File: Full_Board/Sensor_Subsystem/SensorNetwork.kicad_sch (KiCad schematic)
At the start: 32 parts, among them IC5 CD74HC4051PWT, IC6 CD74HC4051PWT, J10 OQ0432500000G, J11 OQ0432500000G, J12 OQ0432500000G, J13 OQ0432500000G, J14 OQ0432500000G, J15 OQ0432500000G, J16 OQ0432500000G, J9 OQ0432500000G

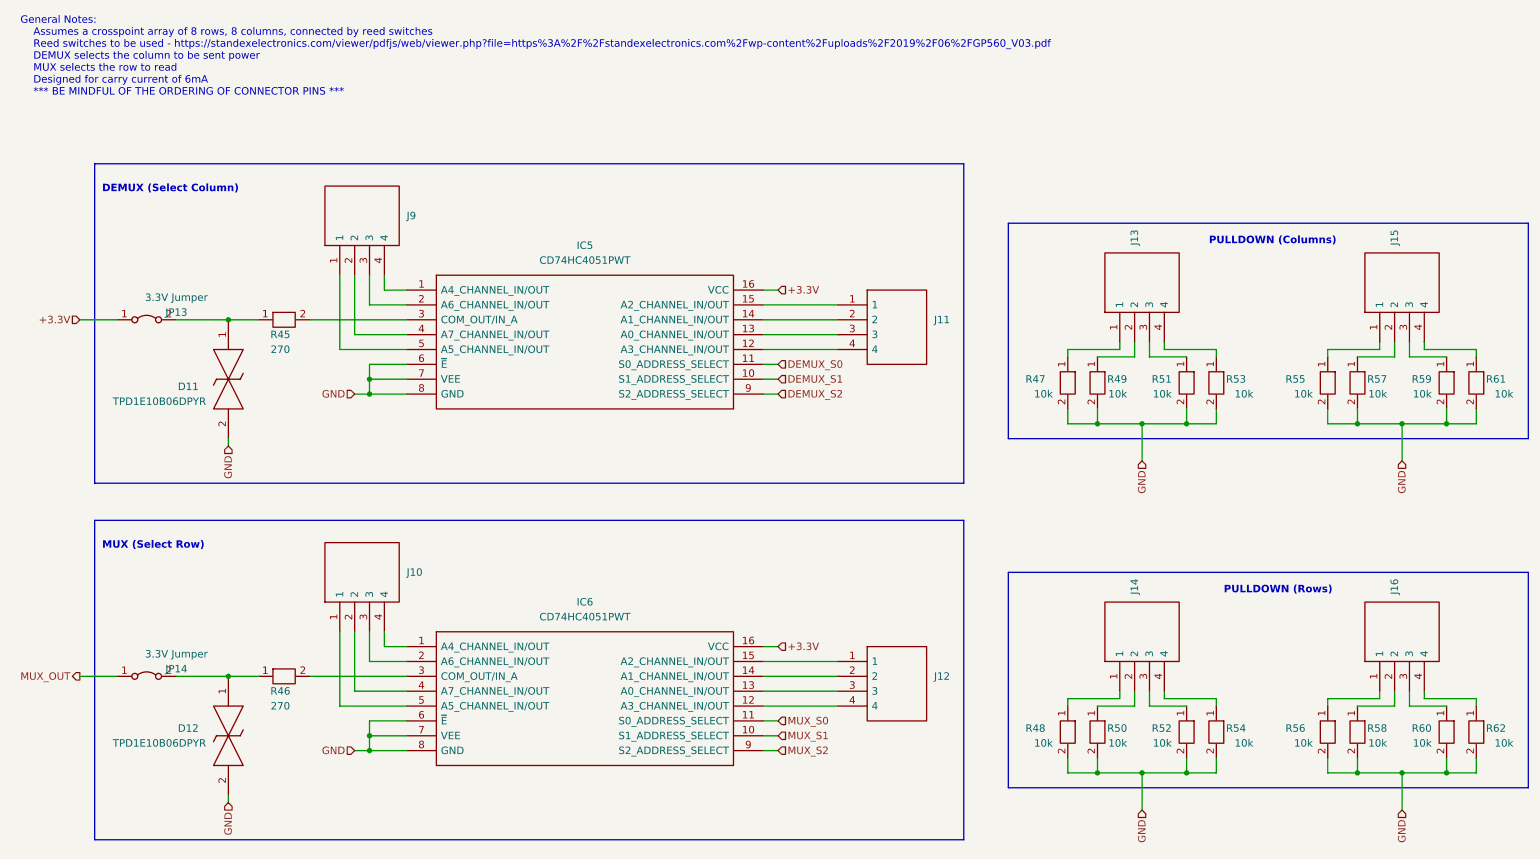
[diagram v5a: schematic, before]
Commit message: Resolve misconfigured components, replace PCB from now completed schematic
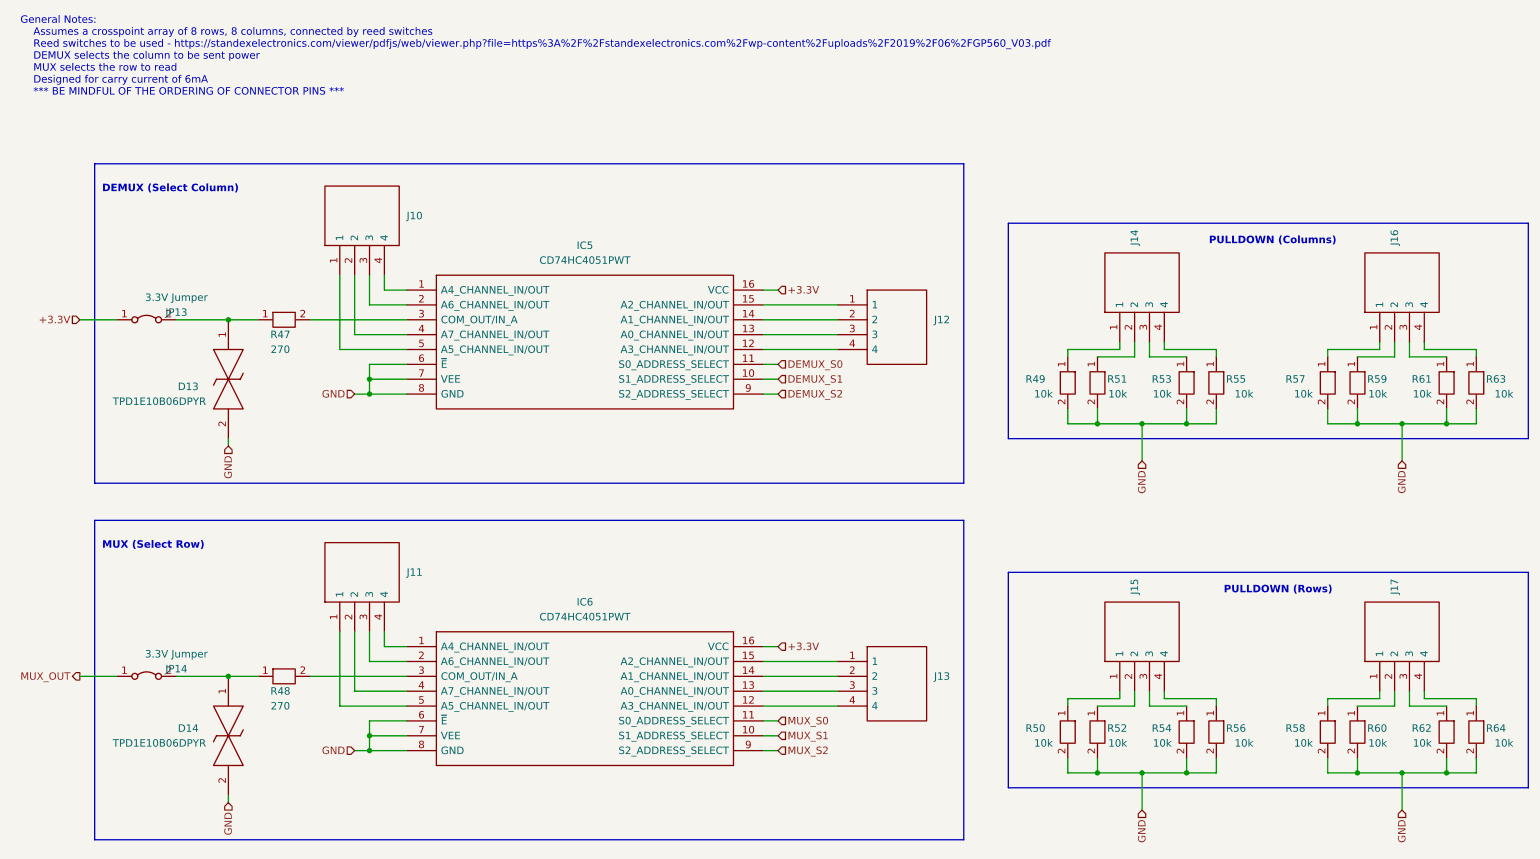
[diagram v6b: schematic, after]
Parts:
- R49: renamed from R47; footprint RESC3225X74N -> RMCF1206FT10K0:RMCF1206FT10K0; Digikey link https://www.digikey.com/en/products/detail/stackpole-electronics-inc/RMCF1206FT10K0/1759669?s=N4IgTCBcDaIEoFkDCAxAjGADANhQFTUwGlMQBdAXyA -> https://www.digikey.com/en/products/detail/stackpole-electronics-inc/RMCF1206FT10K0/1759669
- R50: renamed from R48; footprint RESC3225X74N -> RMCF1206FT10K0:RMCF1206FT10K0; Digikey link https://www.digikey.com/en/products/detail/stackpole-electronics-inc/RMCF1206FT10K0/1759669?s=N4IgTCBcDaIEoFkDCAxAjGADANhQFTUwGlMQBdAXyA -> https://www.digikey.com/en/products/detail/stackpole-electronics-inc/RMCF1206FT10K0/1759669
- R51: renamed from R49; footprint RESC3225X74N -> RMCF1206FT10K0:RMCF1206FT10K0; Digikey link https://www.digikey.com/en/products/detail/stackpole-electronics-inc/RMCF1206FT10K0/1759669?s=N4IgTCBcDaIEoFkDCAxAjGADANhQFTUwGlMQBdAXyA -> https://www.digikey.com/en/products/detail/stackpole-electronics-inc/RMCF1206FT10K0/1759669
- R52: renamed from R50; footprint RESC3225X74N -> RMCF1206FT10K0:RMCF1206FT10K0; Digikey link https://www.digikey.com/en/products/detail/stackpole-electronics-inc/RMCF1206FT10K0/1759669?s=N4IgTCBcDaIEoFkDCAxAjGADANhQFTUwGlMQBdAXyA -> https://www.digikey.com/en/products/detail/stackpole-electronics-inc/RMCF1206FT10K0/1759669
- R53: renamed from R51; footprint RESC3225X74N -> RMCF1206FT10K0:RMCF1206FT10K0; Digikey link https://www.digikey.com/en/products/detail/stackpole-electronics-inc/RMCF1206FT10K0/1759669?s=N4IgTCBcDaIEoFkDCAxAjGADANhQFTUwGlMQBdAXyA -> https://www.digikey.com/en/products/detail/stackpole-electronics-inc/RMCF1206FT10K0/1759669
- R54: renamed from R52; footprint RESC3225X74N -> RMCF1206FT10K0:RMCF1206FT10K0; Digikey link https://www.digikey.com/en/products/detail/stackpole-electronics-inc/RMCF1206FT10K0/1759669?s=N4IgTCBcDaIEoFkDCAxAjGADANhQFTUwGlMQBdAXyA -> https://www.digikey.com/en/products/detail/stackpole-electronics-inc/RMCF1206FT10K0/1759669
- R55: renamed from R53; footprint RESC3225X74N -> RMCF1206FT10K0:RMCF1206FT10K0; Digikey link https://www.digikey.com/en/products/detail/stackpole-electronics-inc/RMCF1206FT10K0/1759669?s=N4IgTCBcDaIEoFkDCAxAjGADANhQFTUwGlMQBdAXyA -> https://www.digikey.com/en/products/detail/stackpole-electronics-inc/RMCF1206FT10K0/1759669
- R56: renamed from R54; footprint RESC3225X74N -> RMCF1206FT10K0:RMCF1206FT10K0; Digikey link https://www.digikey.com/en/products/detail/stackpole-electronics-inc/RMCF1206FT10K0/1759669?s=N4IgTCBcDaIEoFkDCAxAjGADANhQFTUwGlMQBdAXyA -> https://www.digikey.com/en/products/detail/stackpole-electronics-inc/RMCF1206FT10K0/1759669
- R57: renamed from R55; footprint RESC3225X74N -> RMCF1206FT10K0:RMCF1206FT10K0; Digikey link https://www.digikey.com/en/products/detail/stackpole-electronics-inc/RMCF1206FT10K0/1759669?s=N4IgTCBcDaIEoFkDCAxAjGADANhQFTUwGlMQBdAXyA -> https://www.digikey.com/en/products/detail/stackpole-electronics-inc/RMCF1206FT10K0/1759669
- R58: renamed from R56; footprint RESC3225X74N -> RMCF1206FT10K0:RMCF1206FT10K0; Digikey link https://www.digikey.com/en/products/detail/stackpole-electronics-inc/RMCF1206FT10K0/1759669?s=N4IgTCBcDaIEoFkDCAxAjGADANhQFTUwGlMQBdAXyA -> https://www.digikey.com/en/products/detail/stackpole-electronics-inc/RMCF1206FT10K0/1759669
- R59: renamed from R57; footprint RESC3225X74N -> RMCF1206FT10K0:RMCF1206FT10K0; Digikey link https://www.digikey.com/en/products/detail/stackpole-electronics-inc/RMCF1206FT10K0/1759669?s=N4IgTCBcDaIEoFkDCAxAjGADANhQFTUwGlMQBdAXyA -> https://www.digikey.com/en/products/detail/stackpole-electronics-inc/RMCF1206FT10K0/1759669
- R60: renamed from R58; footprint RESC3225X74N -> RMCF1206FT10K0:RMCF1206FT10K0; Digikey link https://www.digikey.com/en/products/detail/stackpole-electronics-inc/RMCF1206FT10K0/1759669?s=N4IgTCBcDaIEoFkDCAxAjGADANhQFTUwGlMQBdAXyA -> https://www.digikey.com/en/products/detail/stackpole-electronics-inc/RMCF1206FT10K0/1759669
- R61: renamed from R59; footprint RESC3225X74N -> RMCF1206FT10K0:RMCF1206FT10K0; Digikey link https://www.digikey.com/en/products/detail/stackpole-electronics-inc/RMCF1206FT10K0/1759669?s=N4IgTCBcDaIEoFkDCAxAjGADANhQFTUwGlMQBdAXyA -> https://www.digikey.com/en/products/detail/stackpole-electronics-inc/RMCF1206FT10K0/1759669
- R62: renamed from R60; footprint RESC3225X74N -> RMCF1206FT10K0:RMCF1206FT10K0; Digikey link https://www.digikey.com/en/products/detail/stackpole-electronics-inc/RMCF1206FT10K0/1759669?s=N4IgTCBcDaIEoFkDCAxAjGADANhQFTUwGlMQBdAXyA -> https://www.digikey.com/en/products/detail/stackpole-electronics-inc/RMCF1206FT10K0/1759669
- R63: renamed from R61; footprint RESC3225X74N -> RMCF1206FT10K0:RMCF1206FT10K0; Digikey link https://www.digikey.com/en/products/detail/stackpole-electronics-inc/RMCF1206FT10K0/1759669?s=N4IgTCBcDaIEoFkDCAxAjGADANhQFTUwGlMQBdAXyA -> https://www.digikey.com/en/products/detail/stackpole-electronics-inc/RMCF1206FT10K0/1759669
- R64: renamed from R62; footprint RESC3225X74N -> RMCF1206FT10K0:RMCF1206FT10K0; Digikey link https://www.digikey.com/en/products/detail/stackpole-electronics-inc/RMCF1206FT10K0/1759669?s=N4IgTCBcDaIEoFkDCAxAjGADANhQFTUwGlMQBdAXyA -> https://www.digikey.com/en/products/detail/stackpole-electronics-inc/RMCF1206FT10K0/1759669
- renumbered D11 to D13, D12 to D14, J9 to J10, J10 to J11, J11 to J12, J12 to J13, J13 to J14, J14 to J15, J15 to J16, J16 to J17, R45 to R47, R46 to R48

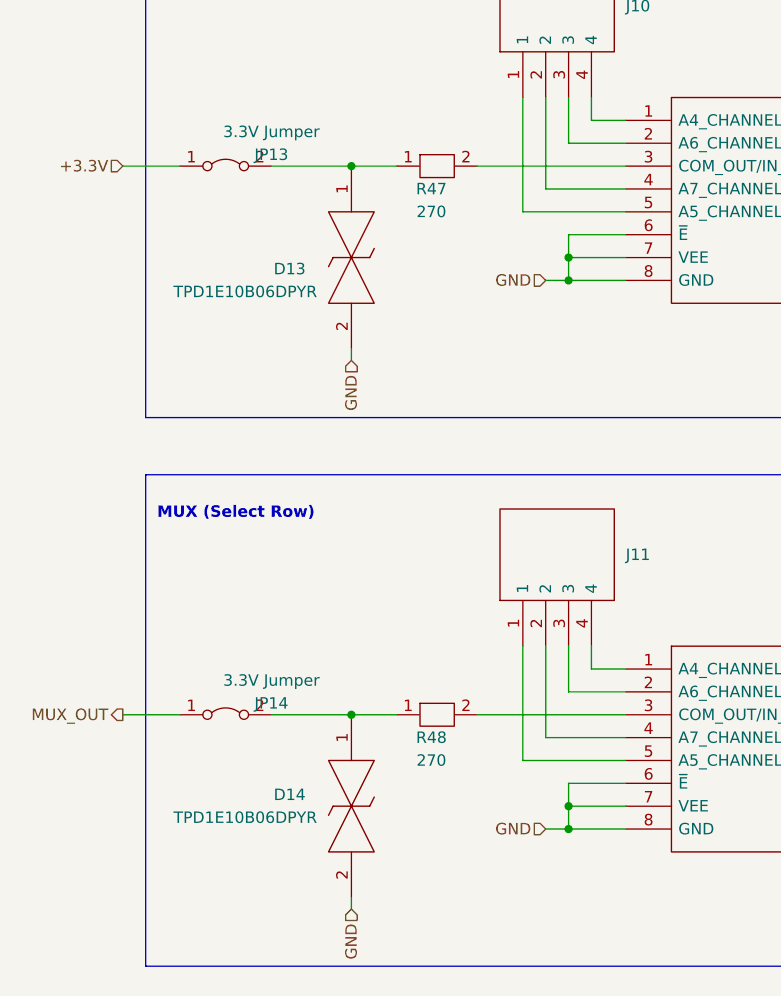
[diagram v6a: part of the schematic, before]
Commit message: Swapped TVS Diodes
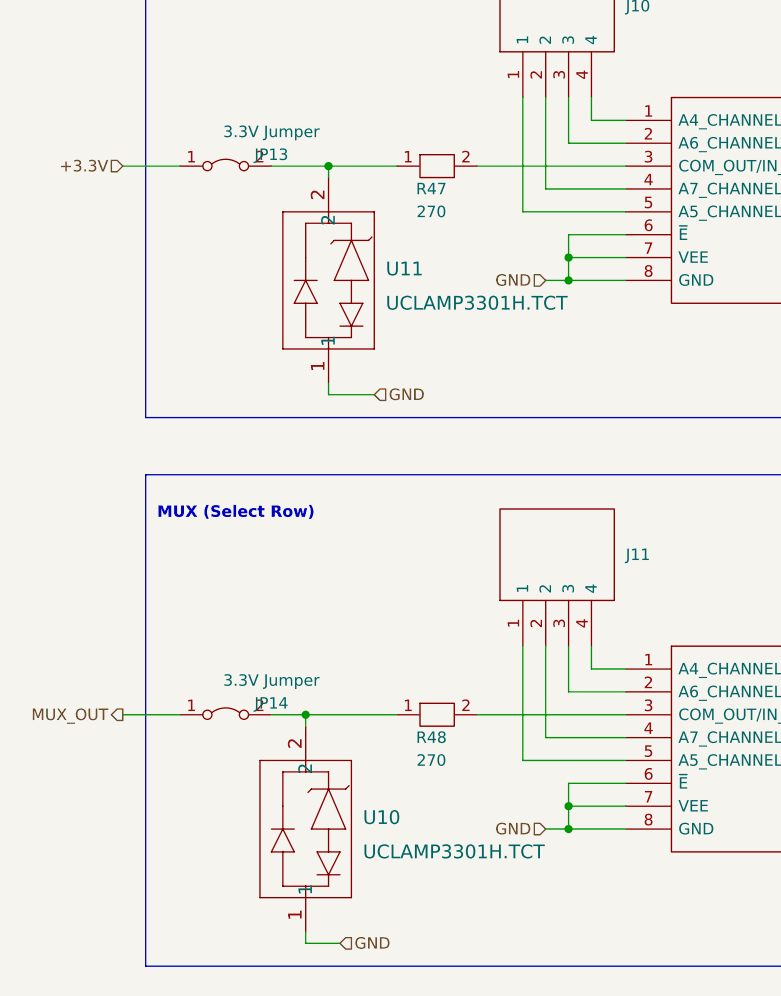
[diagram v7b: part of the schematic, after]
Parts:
- removed D13, D14: TPD1E10B06DPYR, TPD1E10B06DPYR:TPD1E10B06DPYR, symbol TPD1E10B06DPYR:TPD1E10B06DPYR
- added U10, U11: UCLAMP3301H.TCT, SOD_01H.TCT_SEM, symbol UCLAMP3301H-TCT:UCLAMP3301H.TCT
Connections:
- net GND: now also U10.1, U11.1
- net at JP13.2 (B), R47.1: now also U11.2
- net at JP14.2 (B), R48.1: now also U10.2

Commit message: Relayed out the power supply and stepper drivers
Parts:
- U10, U11: footprint SOD_01H.TCT_SEM -> UCLAMP3310H-TCT:UCLAMP3301H.TCT
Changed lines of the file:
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@@
       (effects (font (size 1.524 1.524)) (justify right))
     )
-    (property "Footprint" "SOD_01H.TCT_SEM" (id 2) (at 34.29 77.47 0)
+    (property "Footprint" "UCLAMP3310H-TCT:UCLAMP3301H.TCT" (id 2) (at 34.29 77.47 0)
       (effects (font (size 1.524 1.524)) hide)
     )
@@
     (pin "2")
   )
-  (symbol (lib_id "UCLAMP3301H-TCT:UCLAMP3301H.TCT") (at 46.99 161.29 90) (unit 1)
+  (symbol (lib_name "UCLAMP3301H.TCT_1") (lib_id "UCLAMP3301H-TCT:UCLAMP3301H.TCT") (at 46.99 161.29 90) (unit 1)
     (in_bom yes) (on_board yes) (fields_autoplaced)
     (property "Reference" "U10" (id 0) (at 53.34 139.7 90)
@@
       (effects (font (size 1.524 1.524)) (justify right))
     )
-    (property "Footprint" "SOD_01H.TCT_SEM" (id 2) (at 31.75 138.43 0)
+    (property "Footprint" "UCLAMP3310H-TCT:UCLAMP3301H.TCT" (id 2) (at 31.75 138.43 0)
       (effects (font (size 1.524 1.524)) hide)
     )
